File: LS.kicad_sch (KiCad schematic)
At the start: 5 parts, among them U4 VNLD5160TR-E

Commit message: Rev B
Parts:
- added R21, R22: 4.7k, Hellen:R0603, symbol Device:R
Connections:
- net IN_1: now also R21.2; no longer R9.2, U4.1 (IN1)
- net IN_2: now also R22.2; no longer R10.2, U4.3 (IN2)
- new net: R21.1, R9.2, U4.1 (IN1)
- new net: R10.2, R22.1, U4.3 (IN2)
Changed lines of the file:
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@@
+    (stroke (width 0) (type default))
+  )
+  (wire (pts (xy 48.26 62.23) (xy 55.88 62.23))
     (stroke (width 0) (type default))
   )
@@
     (stroke (width 0) (type default))
   )
+  (wire (pts (xy 48.26 57.15) (xy 55.88 57.15))
+    (stroke (width 0) (type default))
+  )
   (wire (pts (xy 63.5 57.15) (xy 73.66 57.15))
     (stroke (width 0) (type default))
@@
     (stroke (width 0) (type default))
   )
-  (hierarchical_label "IN_1" (shape input) (at 63.5 57.15 180) (fields_autoplaced)
+  (hierarchical_label "IN_1" (shape input) (at 48.26 57.15 180) (fields_autoplaced)
     (effects (font (size 1.27 1.27)) (justify right))
   )
@@
     (effects (font (size 1.27 1.27)) (justify left))
   )
-  (hierarchical_label "IN_2" (shape input) (at 63.5 62.23 180) (fields_autoplaced)
+  (hierarchical_label "IN_2" (shape input) (at 48.26 62.23 180) (fields_autoplaced)
     (effects (font (size 1.27 1.27)) (justify right))
   )
@@
         (path "/b8382448-02ab-4b6d-b574-50f724fc5555/4d1d140e-577f-4c68-bab8-9a91e78a044c"
           (reference "#PWR014") (unit 1)
+        )
+      )
+    )
+  )
+  (symbol (lib_id "Device:R") (at 59.69 57.15 270) (unit 1)
+    (in_bom yes) (on_board yes) (dnp no)
+    (property "Reference" "R21" (at 58.42 54.61 90)
+      (effects (font (size 1.27 1.27)) (justify left))
+    )
+    (property "Value" "4.7k" (at 57.15 57.15 90)
+      (effects (font (size 1.27 1.27)) (justify left))
+    )
+    (property "Footprint" "Hellen:R0603" (at 59.69 55.372 90)
+      (effects (font (size 1.27 1.27)) hide)
+    )
+    (property "Datasheet" "~" (at 59.69 57.15 0)
+      (effects (font (size 1.27 1.27)) hide)
+    )
+    (property "LCSC" "C23162" (at 59.69 57.15 0)
+      (effects (font (size 1.27 1.27)) hide)
+    )
+    (pin "2")
+    (pin "1")
+    (instances
+      (project "PROLT"
+        (path "/b8382448-02ab-4b6d-b574-50f724fc5555/4d1d140e-577f-4c68-bab8-9a91e78a044c"
+          (reference "R21") (unit 1)
         )
       )
@@
         )
       )
+    )
+  )
+  (symbol (lib_id "Device:R") (at 59.69 62.23 270) (unit 1)
+    (in_bom yes) (on_board yes) (dnp no)
+    (property "Reference" "R22" (at 58.42 64.77 90)
+      (effects (font (size 1.27 1.27)) (justify left))
+    )
+    (property "Value" "4.7k" (at 57.15 62.23 90)
+      (effects (font (size 1.27 1.27)) (justify left))
+    )
+    (property "Footprint" "Hellen:R0603" (at 59.69 60.452 90)
+      (effects (font (size 1.27 1.27)) hide)
+    )
+    (property "Datasheet" "~" (at 59.69 62.23 0)
+      (effects (font (size 1.27 1.27)) hide)
+    )
+    (property "LCSC" "C23162" (at 59.69 62.23 0)
+      (effects (font (size 1.27 1.27)) hide)
+    )
+    (pin "2")
+    (pin "1")
+    (instances
+      (project "PROLT"
+        (path "/b8382448-02ab-4b6d-b574-50f724fc5555/4d1d140e-577f-4c68-bab8-9a91e78a044c"
+          (reference "R22") (unit 1)
+        )
+      )

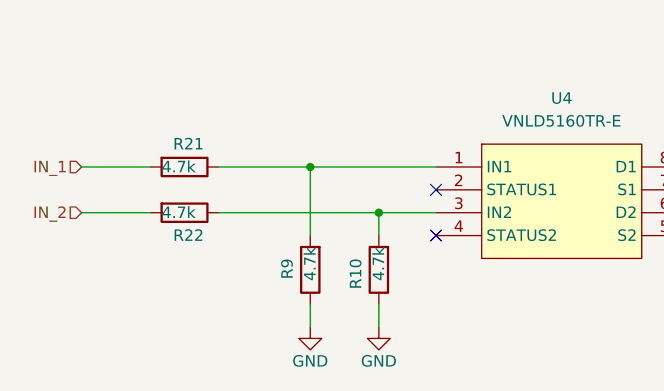
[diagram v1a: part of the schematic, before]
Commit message: Stupid mistake — I ended up making a voltage divider instead of a protection circuit. I'm the best.
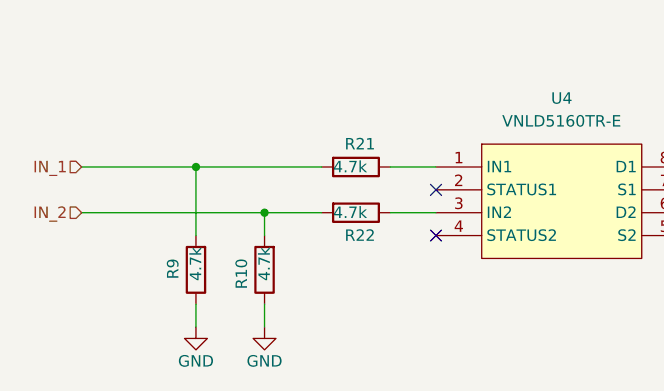
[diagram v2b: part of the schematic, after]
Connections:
- net IN_1: now also R9.2
- net IN_2: now also R10.2
- net at R21.1, U4.1 (IN1): no longer R9.2
- net at R22.1, U4.3 (IN2): no longer R10.2
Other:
- moved on the sheet: R10, R21, R22, R9
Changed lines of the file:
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@@
 (kicad_sch (version 20230121) (generator eeschema)
   (paper "A5")
+  (junction (at 68.58 62.23) (diameter 0) (color 0 0 0 0)
+  )
+  (junction (at 60.96 57.15) (diameter 0) (color 0 0 0 0)
+  )
   (junction (at 120.65 64.77) (diameter 0) (color 0 0 0 0)
   )
   (junction (at 128.27 57.15) (diameter 0) (color 0 0 0 0)
-  )
-  (junction (at 81.28 62.23) (diameter 0) (color 0 0 0 0)
-  )
-  (junction (at 73.66 57.15) (diameter 0) (color 0 0 0 0)
   )
   (junction (at 128.27 62.23) (diameter 0) (color 0 0 0 0)
@@
     (stroke (width 0) (type default))
   )
+  (wire (pts (xy 82.55 57.15) (xy 87.63 57.15))
+    (stroke (width 0) (type default))
+  )
   (wire (pts (xy 138.43 73.66) (xy 146.05 73.66))
     (stroke (width 0) (type default))
@@
     (stroke (width 0) (type default))
   )
-  (wire (pts (xy 81.28 62.23) (xy 87.63 62.23))
+  (wire (pts (xy 48.26 57.15) (xy 60.96 57.15))
+    (stroke (width 0) (type default))
+  )
+  (wire (pts (xy 68.58 62.23) (xy 74.93 62.23))
     (stroke (width 0) (type default))
   )
@@
     (stroke (width 0) (type default))
   )
-  (wire (pts (xy 81.28 72.39) (xy 81.28 74.93))
-    (stroke (width 0) (type default))
-  )
-  (wire (pts (xy 48.26 62.23) (xy 55.88 62.23))
-    (stroke (width 0) (type default))
-  )
-  (wire (pts (xy 73.66 57.15) (xy 73.66 64.77))
+  (wire (pts (xy 82.55 62.23) (xy 87.63 62.23))
+    (stroke (width 0) (type default))
+  )
+  (wire (pts (xy 68.58 72.39) (xy 68.58 74.93))
+    (stroke (width 0) (type default))
+  )
+  (wire (pts (xy 60.96 57.15) (xy 60.96 64.77))
     (stroke (width 0) (type default))
   )
@@
     (stroke (width 0) (type default))
   )
+  (wire (pts (xy 48.26 62.23) (xy 68.58 62.23))
+    (stroke (width 0) (type default))
+  )
   (wire (pts (xy 120.65 59.69) (xy 120.65 64.77))
     (stroke (width 0) (type default))
   )
-  (wire (pts (xy 73.66 72.39) (xy 73.66 74.93))
+  (wire (pts (xy 60.96 72.39) (xy 60.96 74.93))
     (stroke (width 0) (type default))
   )
@@
     (stroke (width 0) (type default))
   )
-  (wire (pts (xy 48.26 57.15) (xy 55.88 57.15))
-    (stroke (width 0) (type default))
-  )
-  (wire (pts (xy 63.5 57.15) (xy 73.66 57.15))
-    (stroke (width 0) (type default))
-  )
   (wire (pts (xy 146.05 48.26) (xy 146.05 45.72))
     (stroke (width 0) (type default))
@@
     (stroke (width 0) (type default))
   )
-  (wire (pts (xy 73.66 57.15) (xy 87.63 57.15))
-    (stroke (width 0) (type default))
-  )
-  (wire (pts (xy 63.5 62.23) (xy 81.28 62.23))
+  (wire (pts (xy 60.96 57.15) (xy 74.93 57.15))
     (stroke (width 0) (type default))
   )
@@
     (stroke (width 0) (type default))
   )
-  (wire (pts (xy 81.28 62.23) (xy 81.28 64.77))
+  (wire (pts (xy 68.58 62.23) (xy 68.58 64.77))
     (stroke (width 0) (type default))
   )
@@
     )
   )
-  (symbol (lib_id "Device:R") (at 59.69 57.15 270) (unit 1)
-    (in_bom yes) (on_board yes) (dnp no)
-    (property "Reference" "R21" (at 58.42 54.61 90)
-      (effects (font (size 1.27 1.27)) (justify left))
-    )
-    (property "Value" "4.7k" (at 57.15 57.15 90)
-      (effects (font (size 1.27 1.27)) (justify left))
-    )
-    (property "Footprint" "Hellen:R0603" (at 59.69 55.372 90)
-      (effects (font (size 1.27 1.27)) hide)
-    )
-    (property "Datasheet" "~" (at 59.69 57.15 0)
-      (effects (font (size 1.27 1.27)) hide)
-    )
-    (property "LCSC" "C23162" (at 59.69 57.15 0)
+  (symbol (lib_id "Device:R") (at 78.74 57.15 270) (unit 1)
+    (in_bom yes) (on_board yes) (dnp no)
+    (property "Reference" "R21" (at 77.47 54.61 90)
+      (effects (font (size 1.27 1.27)) (justify left))
+    )
+    (property "Value" "4.7k" (at 76.2 57.15 90)
+      (effects (font (size 1.27 1.27)) (justify left))
+    )
+    (property "Footprint" "Hellen:R0603" (at 78.74 55.372 90)
+      (effects (font (size 1.27 1.27)) hide)
+    )
+    (property "Datasheet" "~" (at 78.74 57.15 0)
+      (effects (font (size 1.27 1.27)) hide)
+    )
+    (property "LCSC" "C23162" (at 78.74 57.15 0)
       (effects (font (size 1.27 1.27)) hide)
     )
@@
     )
   )
-  (symbol (lib_id "power:GND") (at 81.28 74.93 0) (unit 1)
-    (in_bom yes) (on_board yes) (dnp no)
-    (property "Reference" "#PWR013" (at 81.28 81.28 0)
-      (effects (font (size 1.27 1.27)) hide)
-    )
-    (property "Value" "GND" (at 81.28 78.74 0)
-      (effects (font (size 1.27 1.27)))
-    )
-    (property "Footprint" "" (at 81.28 74.93 0)
-      (effects (font (size 1.27 1.27)) hide)
-    )
-    (property "Datasheet" "" (at 81.28 74.93 0)
+  (symbol (lib_id "power:GND") (at 68.58 74.93 0) (unit 1)
+    (in_bom yes) (on_board yes) (dnp no)
+    (property "Reference" "#PWR013" (at 68.58 81.28 0)
+      (effects (font (size 1.27 1.27)) hide)
+    )
+    (property "Value" "GND" (at 68.58 78.74 0)
+      (effects (font (size 1.27 1.27)))
+    )
+    (property "Footprint" "" (at 68.58 74.93 0)
+      (effects (font (size 1.27 1.27)) hide)
+    )
+    (property "Datasheet" "" (at 68.58 74.93 0)
       (effects (font (size 1.27 1.27)) hide)
     )
@@
     )
   )
-  (symbol (lib_id "Device:R") (at 73.66 68.58 180) (unit 1)
-    (in_bom yes) (on_board yes) (dnp no)
-    (property "Reference" "R9" (at 71.12 67.31 90)
-      (effects (font (size 1.27 1.27)) (justify left))
-    )
-    (property "Value" "4.7k" (at 73.66 66.04 90)
-      (effects (font (size 1.27 1.27)) (justify left))
-    )
-    (property "Footprint" "Hellen:R0603" (at 75.438 68.58 90)
-      (effects (font (size 1.27 1.27)) hide)
-    )
-    (property "Datasheet" "~" (at 73.66 68.58 0)
-      (effects (font (size 1.27 1.27)) hide)
-    )
-    (property "LCSC" "C23162" (at 73.66 68.58 0)
+  (symbol (lib_id "Device:R") (at 60.96 68.58 180) (unit 1)
+    (in_bom yes) (on_board yes) (dnp no)
+    (property "Reference" "R9" (at 58.42 67.31 90)
+      (effects (font (size 1.27 1.27)) (justify left))
+    )
+    (property "Value" "4.7k" (at 60.96 66.04 90)
+      (effects (font (size 1.27 1.27)) (justify left))
+    )
+    (property "Footprint" "Hellen:R0603" (at 62.738 68.58 90)
+      (effects (font (size 1.27 1.27)) hide)
+    )
+    (property "Datasheet" "~" (at 60.96 68.58 0)
+      (effects (font (size 1.27 1.27)) hide)
+    )
+    (property "LCSC" "C23162" (at 60.96 68.58 0)
       (effects (font (size 1.27 1.27)) hide)
     )
@@
     )
   )
-  (symbol (lib_id "Device:R") (at 81.28 68.58 180) (unit 1)
-    (in_bom yes) (on_board yes) (dnp no)
-    (property "Reference" "R10" (at 78.74 67.31 90)
-      (effects (font (size 1.27 1.27)) (justify left))
-    )
-    (property "Value" "4.7k" (at 81.28 66.04 90)
-      (effects (font (size 1.27 1.27)) (justify left))
-    )
-    (property "Footprint" "Hellen:R0603" (at 83.058 68.58 90)
-      (effects (font (size 1.27 1.27)) hide)
-    )
-    (property "Datasheet" "~" (at 81.28 68.58 0)
-      (effects (font (size 1.27 1.27)) hide)
-    )
-    (property "LCSC" "C23162" (at 81.28 68.58 0)
+  (symbol (lib_id "Device:R") (at 68.58 68.58 180) (unit 1)
+    (in_bom yes) (on_board yes) (dnp no)
+    (property "Reference" "R10" (at 66.04 67.31 90)
+      (effects (font (size 1.27 1.27)) (justify left))
+    )
+    (property "Value" "4.7k" (at 68.58 66.04 90)
+      (effects (font (size 1.27 1.27)) (justify left))
+    )
+    (property "Footprint" "Hellen:R0603" (at 70.358 68.58 90)
+      (effects (font (size 1.27 1.27)) hide)
+    )
+    (property "Datasheet" "~" (at 68.58 68.58 0)
+      (effects (font (size 1.27 1.27)) hide)
+    )
+    (property "LCSC" "C23162" (at 68.58 68.58 0)
       (effects (font (size 1.27 1.27)) hide)
     )
@@
     )
   )
-  (symbol (lib_id "Device:R") (at 59.69 62.23 270) (unit 1)
-    (in_bom yes) (on_board yes) (dnp no)
-    (property "Reference" "R22" (at 58.42 64.77 90)
-      (effects (font (size 1.27 1.27)) (justify left))
-    )
-    (property "Value" "4.7k" (at 57.15 62.23 90)
-      (effects (font (size 1.27 1.27)) (justify left))
-    )
-    (property "Footprint" "Hellen:R0603" (at 59.69 60.452 90)
-      (effects (font (size 1.27 1.27)) hide)
-    )
-    (property "Datasheet" "~" (at 59.69 62.23 0)
-      (effects (font (size 1.27 1.27)) hide)
-    )
-    (property "LCSC" "C23162" (at 59.69 62.23 0)
+  (symbol (lib_id "Device:R") (at 78.74 62.23 270) (unit 1)
+    (in_bom yes) (on_board yes) (dnp no)
+    (property "Reference" "R22" (at 77.47 64.77 90)
+      (effects (font (size 1.27 1.27)) (justify left))
+    )
+    (property "Value" "4.7k" (at 76.2 62.23 90)
+      (effects (font (size 1.27 1.27)) (justify left))
+    )
+    (property "Footprint" "Hellen:R0603" (at 78.74 60.452 90)
+      (effects (font (size 1.27 1.27)) hide)
+    )
+    (property "Datasheet" "~" (at 78.74 62.23 0)
+      (effects (font (size 1.27 1.27)) hide)
+    )
+    (property "LCSC" "C23162" (at 78.74 62.23 0)
       (effects (font (size 1.27 1.27)) hide)
     )
@@
     )
   )
-  (symbol (lib_id "power:GND") (at 73.66 74.93 0) (unit 1)
-    (in_bom yes) (on_board yes) (dnp no)
-    (property "Reference" "#PWR012" (at 73.66 81.28 0)
-      (effects (font (size 1.27 1.27)) hide)
-    )
-    (property "Value" "GND" (at 73.66 78.74 0)
-      (effects (font (size 1.27 1.27)))
-    )
-    (property "Footprint" "" (at 73.66 74.93 0)
-      (effects (font (size 1.27 1.27)) hide)
-    )
-    (property "Datasheet" "" (at 73.66 74.93 0)
-      (effects (font (size 1.27 1.27)) hide)
-    )
+  (symbol (lib_id "power:GND") (at 60.96 74.93 0) (unit 1)
+    (in_bom yes) (on_board yes) (dnp no)
+    (property "Reference" "#PWR012" (at 60.96 81.28 0)
+      (effects (font (size 1.27 1.27)) hide)
+    )
+    (property "Value" "GND" (at 60.96 78.74 0)
+      (effects (font (size 1.27 1.27)))
+    )
+    (property "Footprint" "" (at 60.96 74.93 0)
+      (effects (font (size 1.27 1.27)) hide)
+    )
+    (property "Datasheet" "" (at 60.96 74.93 0)
+      (effects (font (size 1.27 1.27)) hide)
+    )

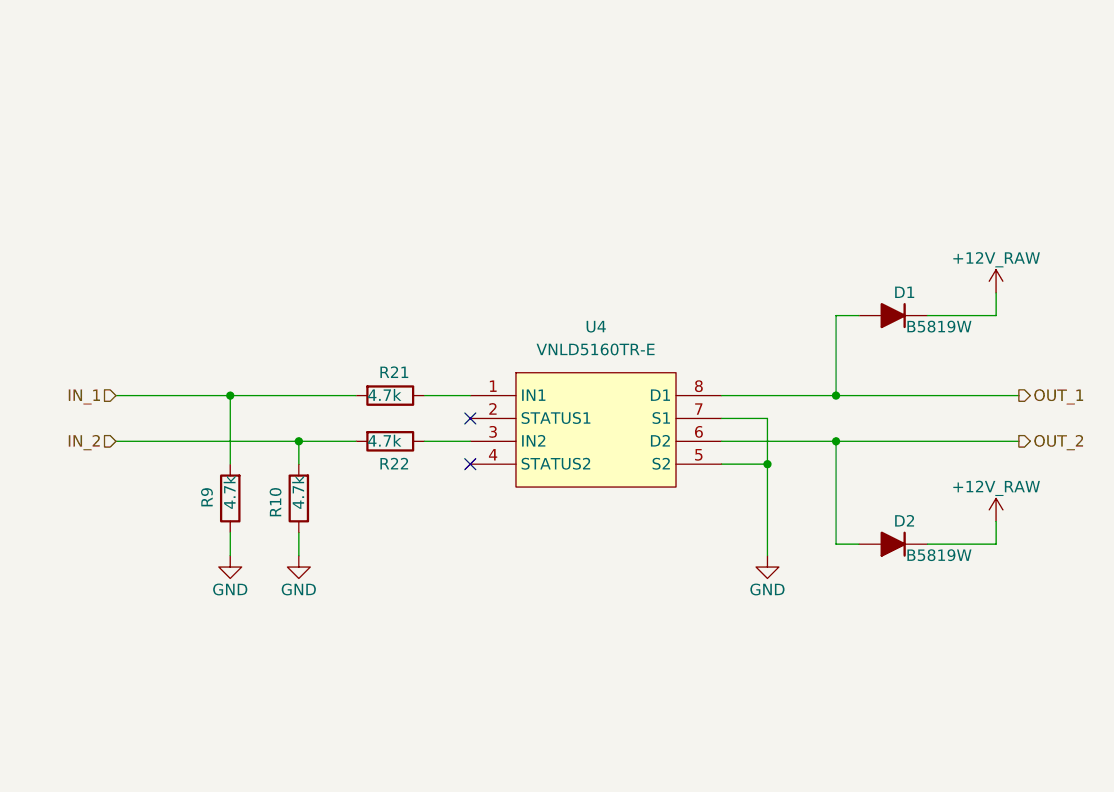
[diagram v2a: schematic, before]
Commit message: Rev E
Back to VNLD5160TR-E, 1 channel per injector now
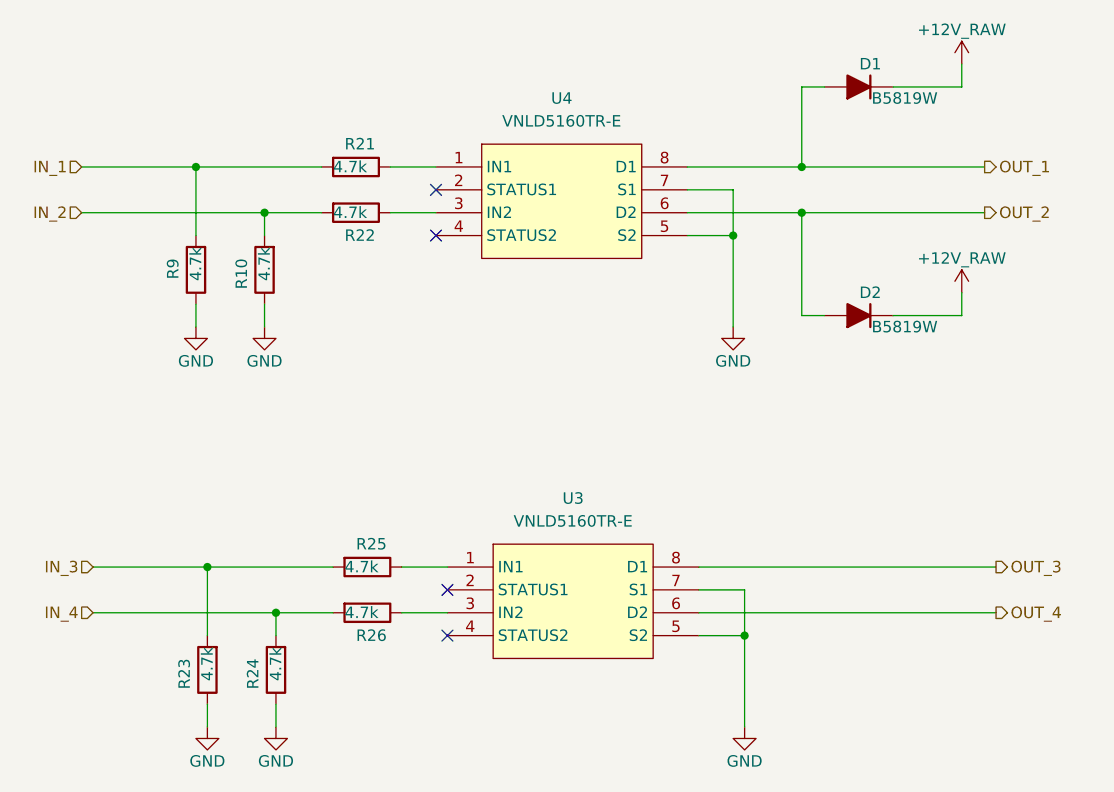
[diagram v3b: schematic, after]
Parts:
- added R23, R24, R25, R26: 4.7k, Hellen:R0603, symbol Device:R
- added U3: VNLD5160TR-E, Package_SO:SOIC-8_3.9x4.9mm_P1.27mm, symbol chips:VNLD5160
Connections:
- net GND: now also R23.1, R24.1, U3.5 (S2), U3.7 (S1)
- new net: R25.1, U3.1 (IN1)
- new net: R26.1, U3.3 (IN2)
- new net IN_3: R23.2, R25.2
- new net IN_4: R24.2, R26.2
- new net OUT_3: U3.8 (D1)
- new net OUT_4: U3.6 (D2)
- no-connect marks 2 -> 4
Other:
- moved on the sheet: D1, D2, R10, R21, R22, R9, U4
